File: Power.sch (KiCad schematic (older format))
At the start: 27 parts, among them IC2 TPS73633, IC3 MCP73831/2-OT, IC4 TPS73618, IC5 MCP1640-SOT, J6 Battery, Q1 Q_PMOS_GSD, SW2 Charge select

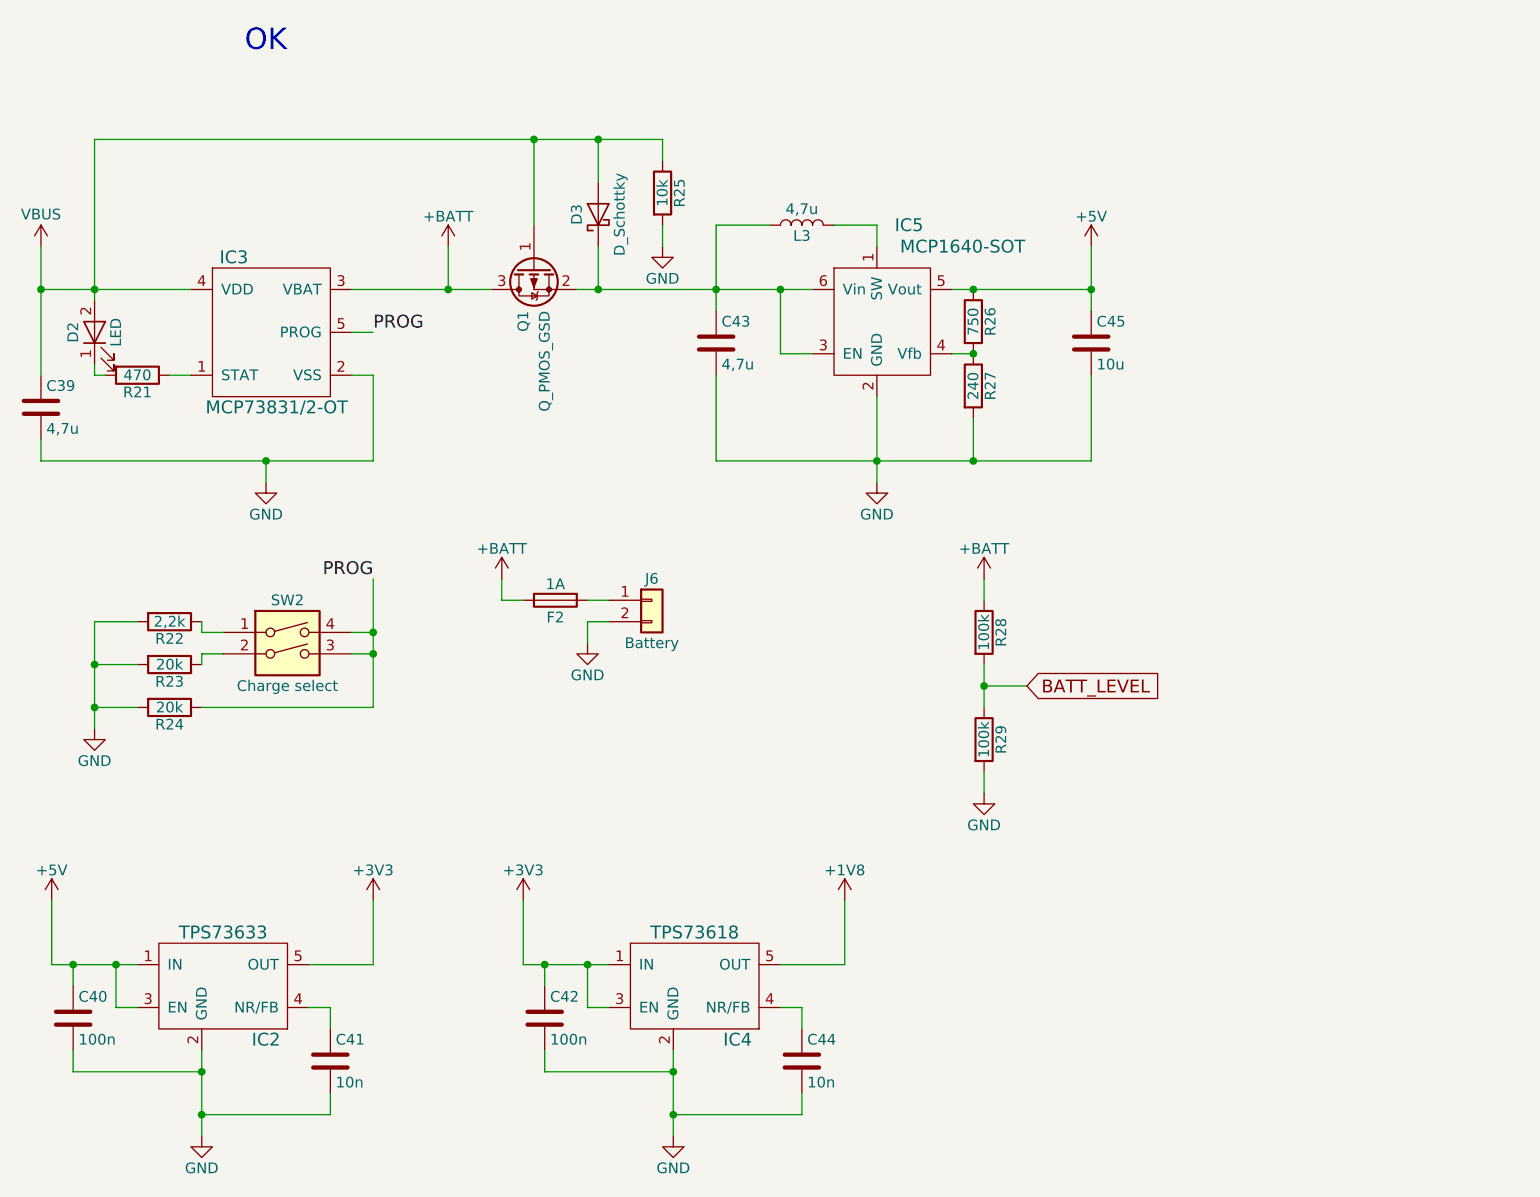
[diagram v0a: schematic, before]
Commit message: Board should be ok. Bargraph leds yet to do.
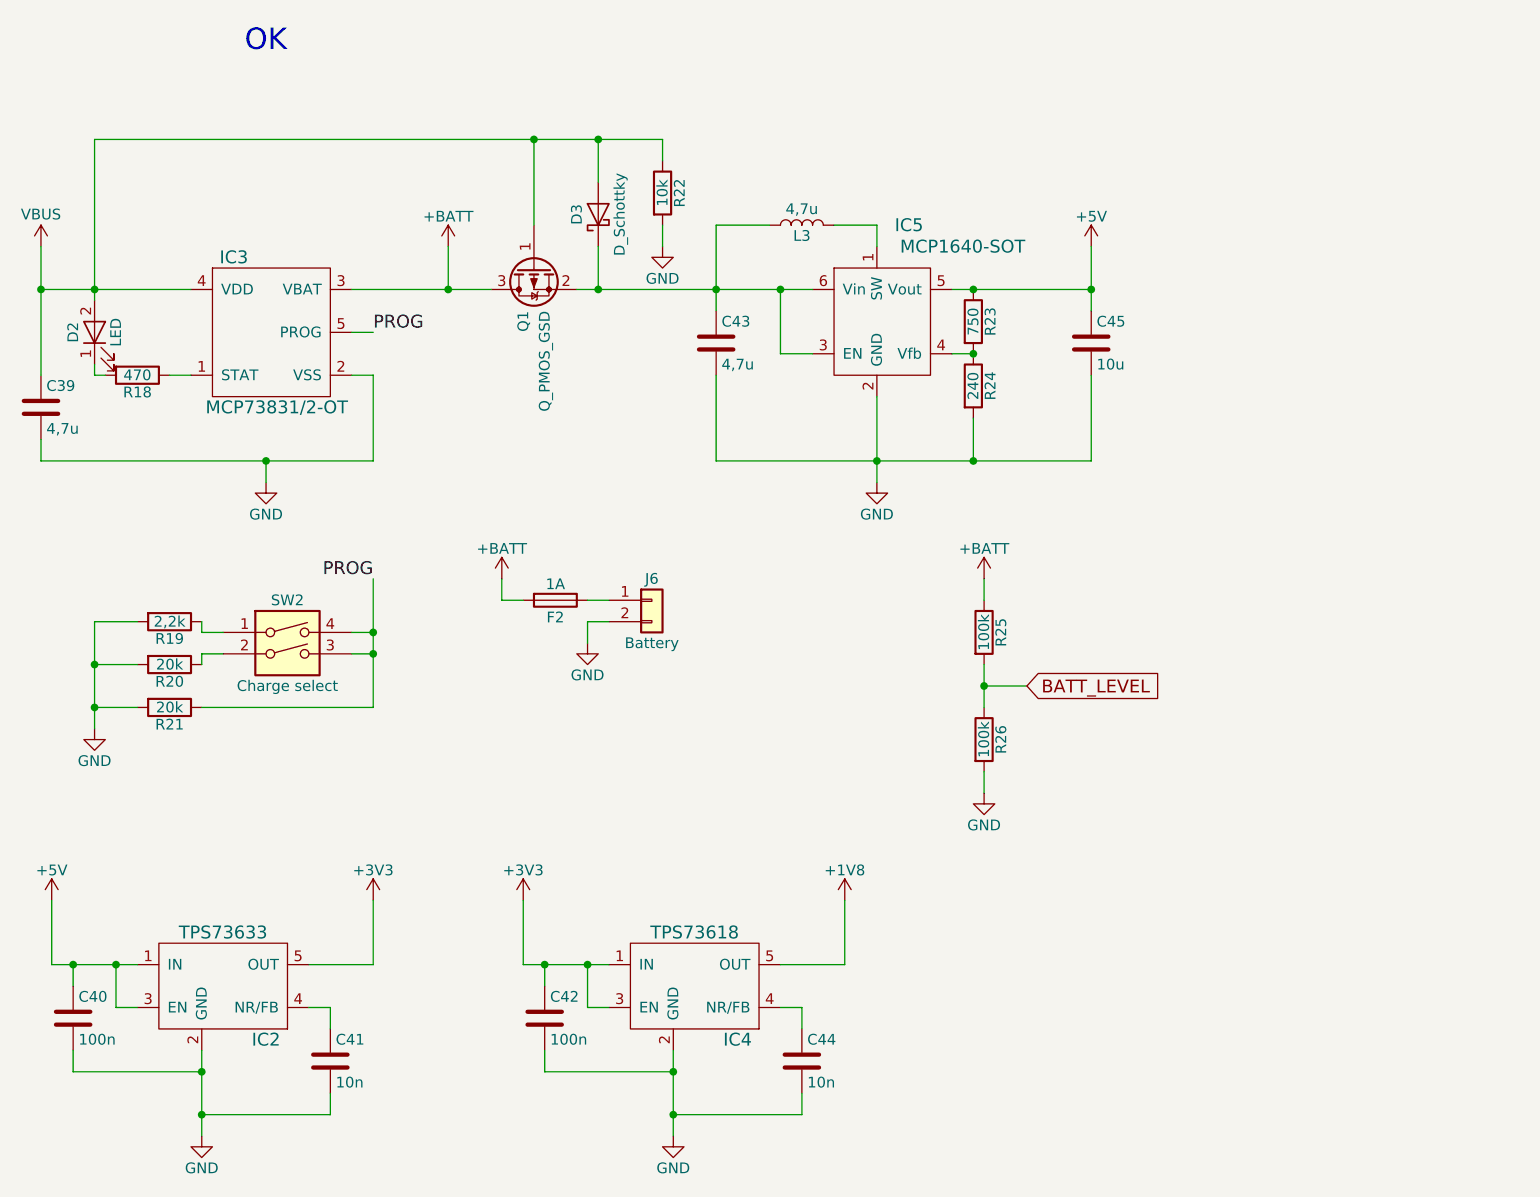
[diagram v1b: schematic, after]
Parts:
- renumbered R21 to R18, R22 to R19, R23 to R20, R24 to R21, R25 to R22, R26 to R23, R27 to R24, R28 to R25, R29 to R26
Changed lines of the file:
@@
 $EndComp
 $Comp
-L R R21
+L R R18
 U 1 1 59A99A93
 P 1400 2250
-F 0 "R21" V 1480 2250 50  0000 C CNN
+F 0 "R18" V 1480 2250 50  0000 C CNN
 F 1 "470" V 1400 2250 50  0000 C CNN
 F 2 "Resistors_SMD:R_0603" V 1330 2250 50  0001 C CNN
@@
 PROG
 $Comp
-L R R22
+L R R19
 U 1 1 59A9ACBF
 P 1550 3400
-F 0 "R22" V 1630 3400 50  0000 C CNN
+F 0 "R19" V 1630 3400 50  0000 C CNN
 F 1 "2,2k" V 1550 3400 50  0000 C CNN
 F 2 "Resistors_SMD:R_0603" V 1480 3400 50  0001 C CNN
@@
 $EndComp
 $Comp
-L R R23
+L R R20
 U 1 1 59A9AD20
 P 1550 3600
-F 0 "R23" V 1630 3600 50  0000 C CNN
+F 0 "R20" V 1630 3600 50  0000 C CNN
 F 1 "20k" V 1550 3600 50  0000 C CNN
 F 2 "Resistors_SMD:R_0603" V 1480 3600 50  0001 C CNN
@@
 $EndComp
 $Comp
-L R R24
+L R R21
 U 1 1 59A9AD49
 P 1550 3800
-F 0 "R24" V 1630 3800 50  0000 C CNN
+F 0 "R21" V 1630 3800 50  0000 C CNN
 F 1 "20k" V 1550 3800 50  0000 C CNN
 F 2 "Resistors_SMD:R_0603" V 1480 3800 50  0001 C CNN
@@
 	5850 1650 5850 1950
 $Comp
-L R R26
+L R R23
 U 1 1 59AAA80E
 P 5300 2000
-F 0 "R26" V 5380 2000 50  0000 C CNN
+F 0 "R23" V 5380 2000 50  0000 C CNN
 F 1 "750" V 5300 2000 50  0000 C CNN
 F 2 "Resistors_SMD:R_0603" V 5230 2000 50  0001 C CNN
@@
 $EndComp
 $Comp
-L R R27
+L R R24
 U 1 1 59AAA96F
 P 5300 2300
-F 0 "R27" V 5380 2300 50  0000 C CNN
+F 0 "R24" V 5380 2300 50  0000 C CNN
 F 1 "240" V 5300 2300 50  0000 C CNN
 F 2 "Resistors_SMD:R_0603" V 5230 2300 50  0001 C CNN
@@
 Connection ~ 3550 1850
 $Comp
-L R R25
+L R R22
 U 1 1 59B0680D
 P 3850 1400
-F 0 "R25" V 3930 1400 50  0000 C CNN
+F 0 "R22" V 3930 1400 50  0000 C CNN
 F 1 "10k" V 3850 1400 50  0000 C CNN
 F 2 "Resistors_SMD:R_0603" V 3780 1400 50  0001 C CNN
@@
 $EndComp
 $Comp
-L R R28
+L R R25
 U 1 1 59B0BDB8
 P 5350 3450
-F 0 "R28" V 5430 3450 50  0000 C CNN
+F 0 "R25" V 5430 3450 50  0000 C CNN
 F 1 "100k" V 5350 3450 50  0000 C CNN
 F 2 "Resistors_SMD:R_0603" V 5280 3450 50  0001 C CNN
@@
 $EndComp
 $Comp
-L R R29
+L R R26
 U 1 1 59B0BF72
 P 5350 3950
-F 0 "R29" V 5430 3950 50  0000 C CNN
+F 0 "R26" V 5430 3950 50  0000 C CNN
 F 1 "100k" V 5350 3950 50  0000 C CNN
 F 2 "Resistors_SMD:R_0603" V 5280 3950 50  0001 C CNN

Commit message: Board modified after ckecking. Ready for fab, just need to create gerber, position and components files.
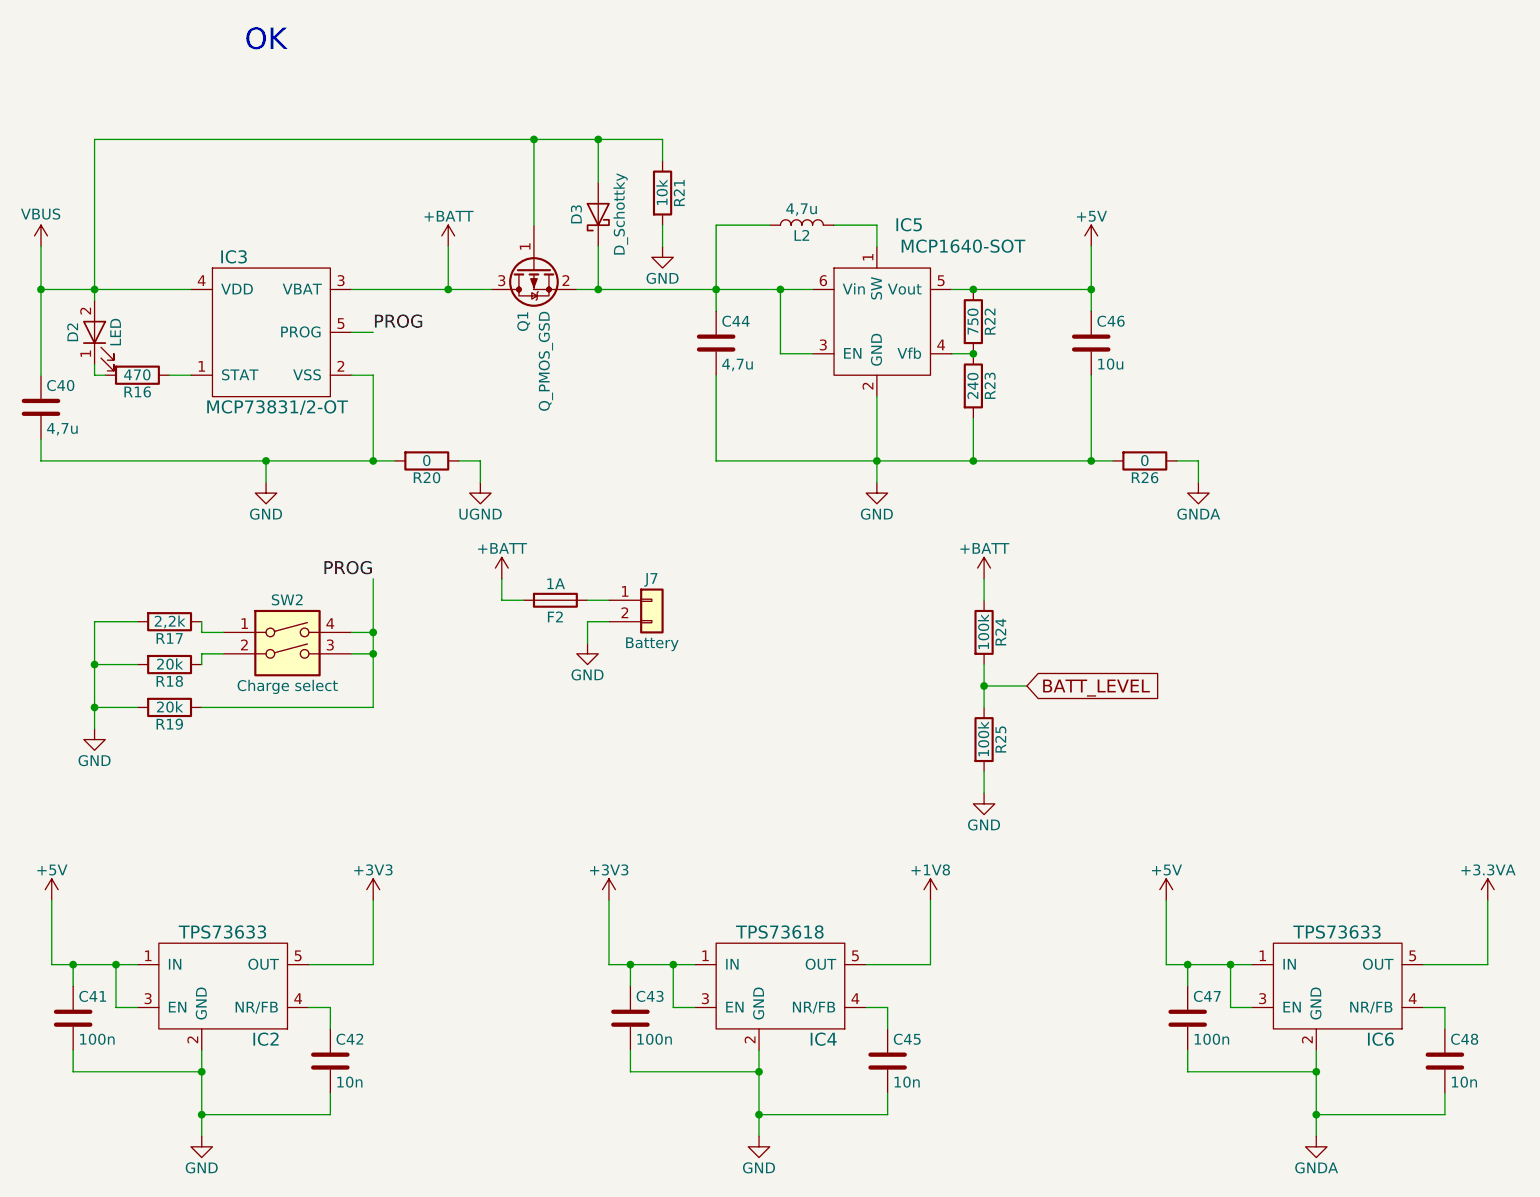
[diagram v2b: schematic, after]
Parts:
- added C47: 100n, Capacitors_SMD:C_0603, symbol C
- added C48: 10n, Capacitors_SMD:C_0603, symbol C
- added IC6: TPS73633, TO_SOT_Packages_SMD:SOT-23-5, symbol TPS736xx
- added R20, R26: 0, Resistors_SMD:R_0603, symbol R
- L2: renamed from L3; footprint Inductors_SMD:L_Vishay_IHLP-1212 -> Inductors_SMD:L_Vishay_IHLP-1616
- renumbered C39 to C40, C40 to C41, C41 to C42, C42 to C43, C43 to C44, C44 to C45, C45 to C46, J6 to J7, R18 to R16, R19 to R17, R20 to R18, R21 to R19, R22 to R21, R23 to R22, R24 to R23, R25 to R24, R26 to R25
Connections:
- net +5V: now also C47.1, IC6.1 (IN), IC6.3 (EN)
- net GND: now also R20.2, R26.2
- new net: C48.1, IC6.4 (NR/FB)
- new net +3.3VA: IC6.5 (OUT)
- new net GNDA: C47.2, C48.2, IC6.2 (GND), R26.1
- new net UGND: R20.1
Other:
- moved on the sheet: C43, C45, IC4

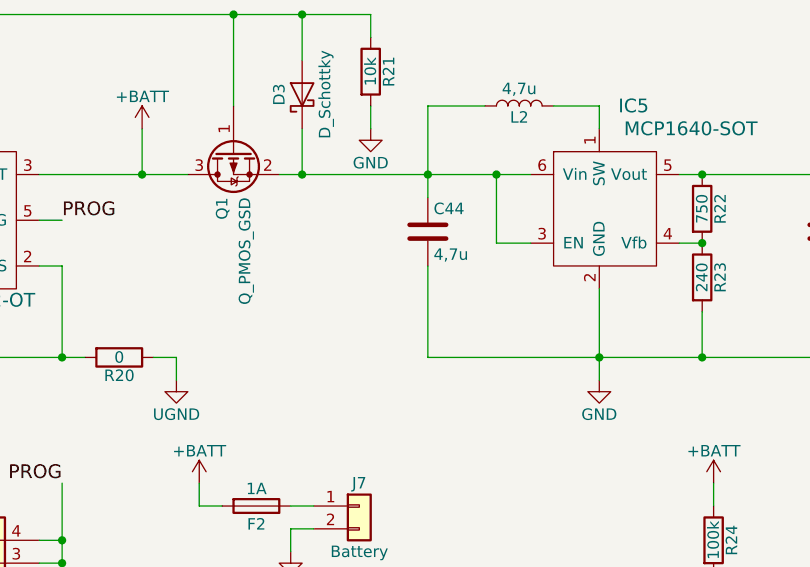
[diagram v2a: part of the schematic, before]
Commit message: Updated project with connector for main power switch. Modified fabrication files.
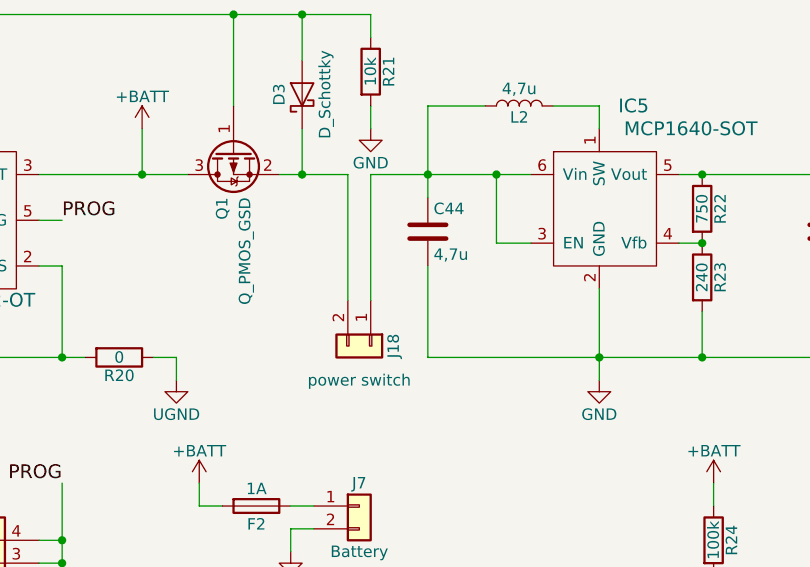
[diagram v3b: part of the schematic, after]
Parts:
- added J18: power switch, Pin_Headers:Pin_Header_Straight_1x02_Pitch2.54mm, symbol Conn_01x02
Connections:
- net at C44.1, IC5.3 (EN), IC5.6 (Vin)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: now also J18.1 (Pin_1); no longer D3.1 (K), Q1.2 (S)
- new net: D3.1 (K), J18.2 (Pin_2), Q1.2 (S)
